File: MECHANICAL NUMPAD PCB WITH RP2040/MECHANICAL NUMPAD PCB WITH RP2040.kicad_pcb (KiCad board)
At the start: 4 copper layers, 76.2 x 95.2 mm, 46 parts, among them IC2 RP2040_QFN56, SW1 SW_Push, SW10 SW_Push, SW11 SW_Push, SW12 SW_Push, SW13 SW_Push, SW14 SW_Push, SW15 SW_Push, SW16 SW_Push, SW17 SW_Push, SW18 SW_Push, SW19 SW_Push, SW2 SW_Push, SW20 SW_Push, SW3 SW_Push, SW4 SW_Push, SW5 SW_Push, SW6 SW_Push, SW7 SW_Push, SW8 SW_Push, SW9 SW_Push, Y1 12MHZ

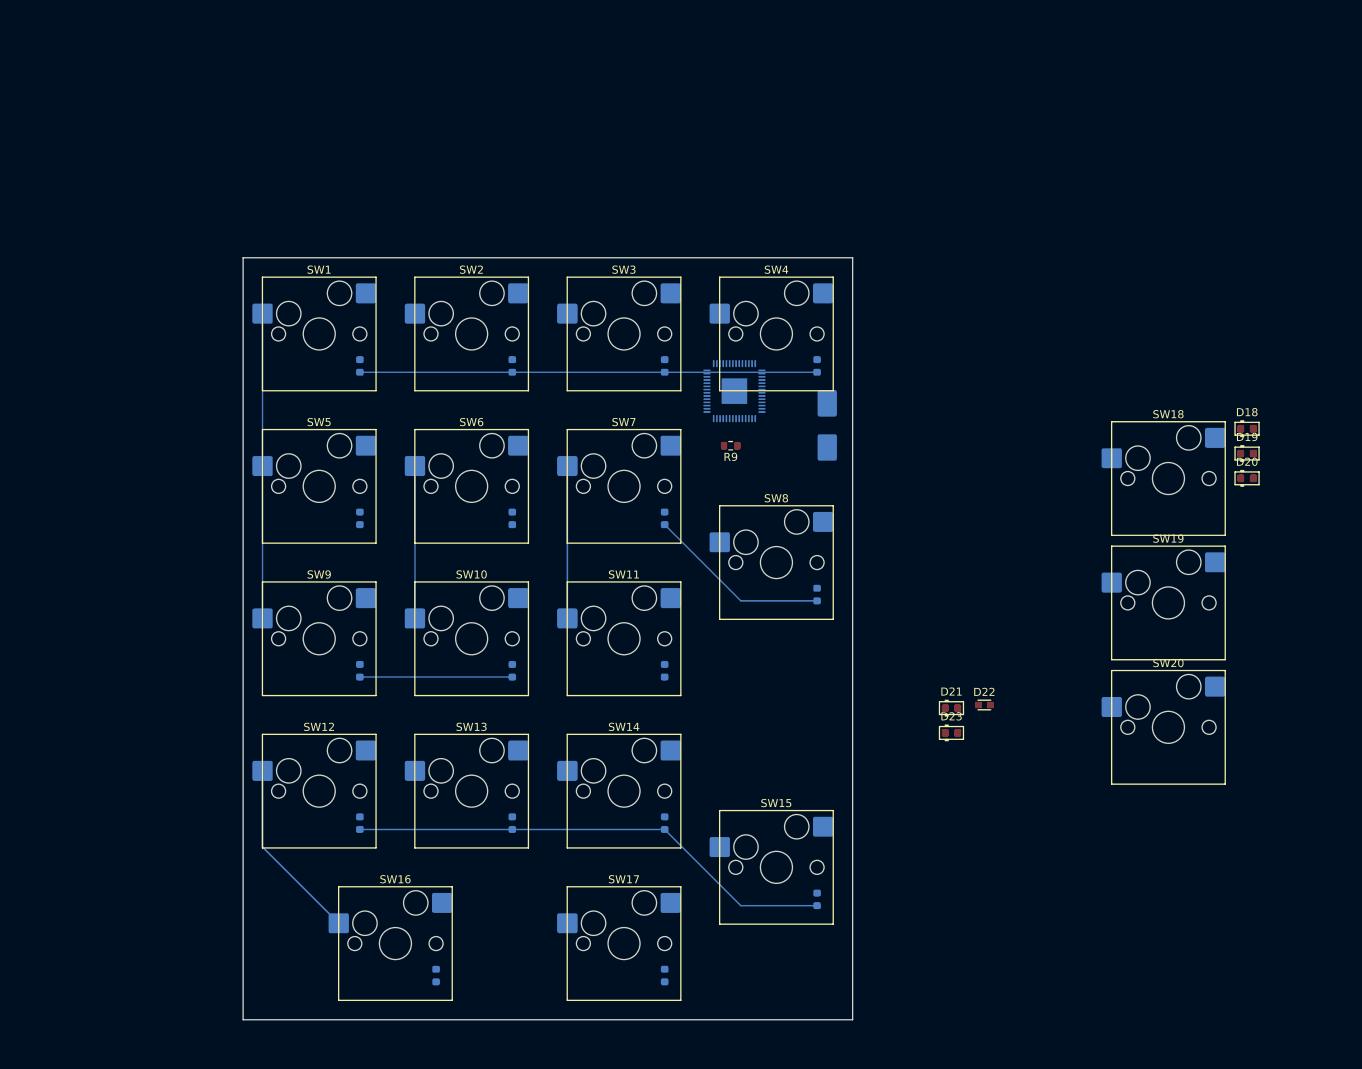
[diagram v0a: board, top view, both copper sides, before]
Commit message: Added footprints
Assigned footprints to all components, learned about bulk schematic symbol editing
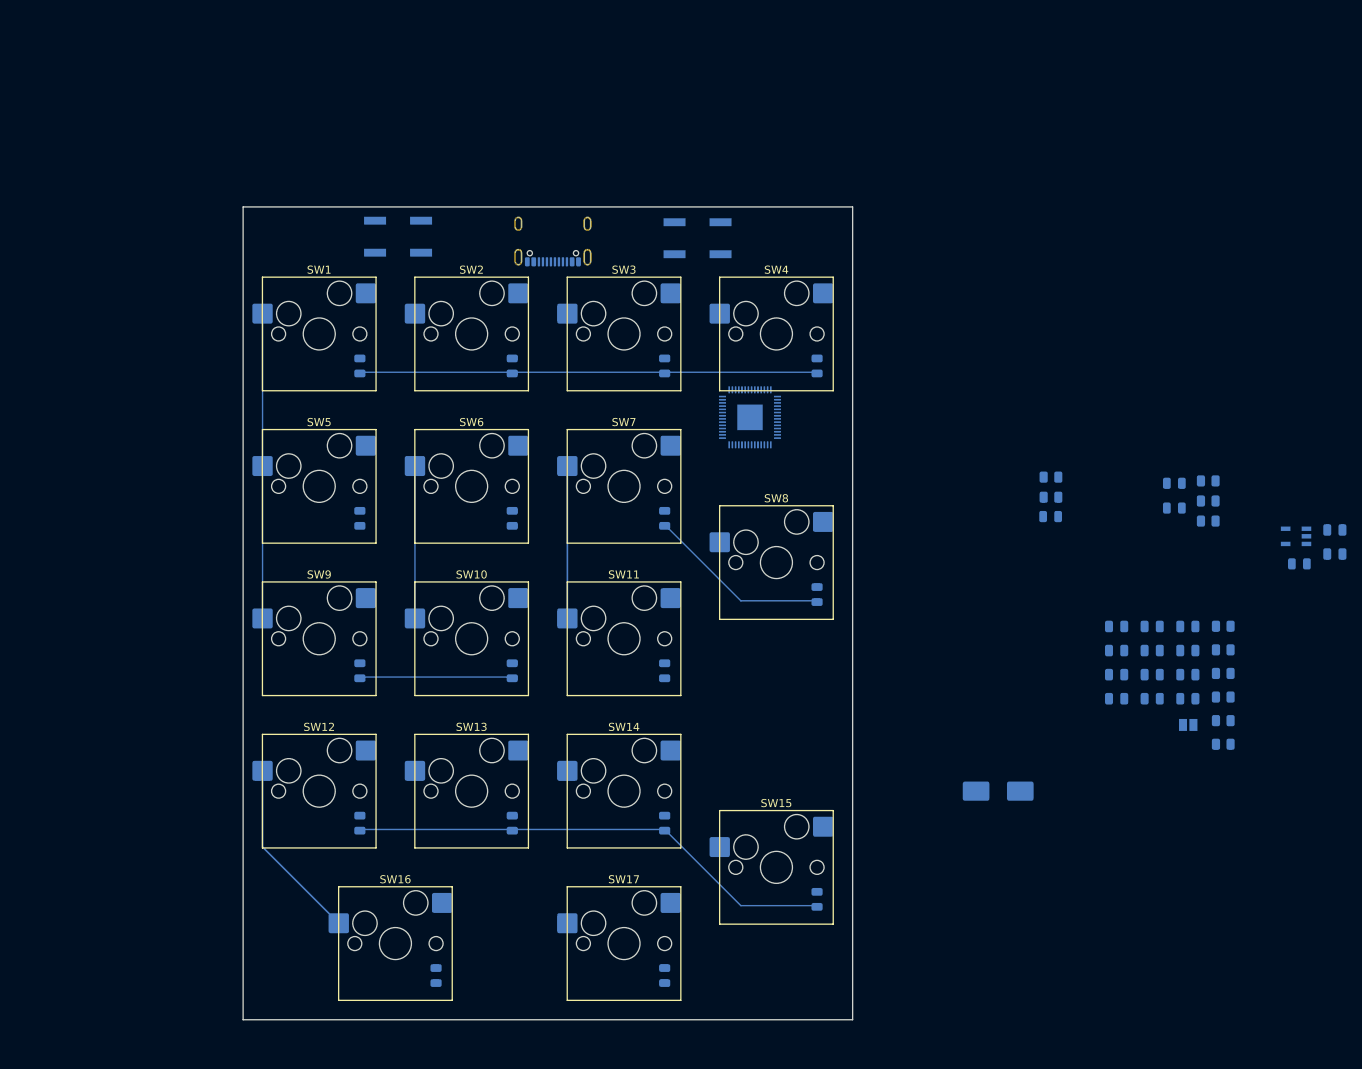
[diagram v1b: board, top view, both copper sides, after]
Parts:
- removed D18, D19, D20: CD4148WT, PCM_Diode_SMD_AKL:D_0603_1608Metric
- removed SW18, SW19, SW20: SW_Push, PCM_Switch_Keyboard_Hotswap_Kailh:SW_Hotswap_Kailh_MX_1.00u
- added C10: 1uF, Capacitor_SMD:C_0805_2012Metric, B.Cu at (146.7, 80.7)
- added C11: 0.1uF, Capacitor_SMD:C_0805_2012Metric, B.Cu at (146.7, 83.7)
- added C12: 1uF, Capacitor_SMD:C_0805_2012Metric, B.Cu at (142.2, 74.7)
- added C13: 0.1uF, Capacitor_SMD:C_0805_2012Metric, B.Cu at (142.2, 77.7)
- added C14: 0.1uF, Capacitor_SMD:C_0805_2012Metric, B.Cu at (142.2, 80.7)
- added C15: 1uF, Capacitor_SMD:C_0805_2012Metric, B.Cu at (142.2, 83.7)
- added C16: 0.1uF, Capacitor_SMD:C_0805_2012Metric, B.Cu at (137.8, 74.7)
- added C17: 0.1uF, Capacitor_SMD:C_0805_2012Metric, B.Cu at (137.8, 77.7)
- added C19: 22pF, Capacitor_SMD:C_0805_2012Metric, B.Cu at (137.8, 80.7)
- added C20: 22pF, Capacitor_SMD:C_0805_2012Metric, B.Cu at (137.8, 83.7)
- added C6: 10µF, Capacitor_SMD:C_0805_2012Metric, B.Cu at (165.1, 62.6)
- added C7: 0.1uF, Capacitor_SMD:C_0805_2012Metric, B.Cu at (146.7, 74.7)
- added C8: 10µF, Capacitor_SMD:C_0805_2012Metric, B.Cu at (165.1, 65.6)
- added C9: 0.1uF, Capacitor_SMD:C_0805_2012Metric, B.Cu at (146.7, 77.7)
- added J1: USB_C_Receptacle_USB2.0_16P, Connector_USB:USB_C_Receptacle_GCT_USB4105-xx-A_16P_TopMnt_Horizontal, B.Cu at (67.3, 25.4)
- added R1: 5.1K, Resistor_SMD:R_0805_2012Metric, B.Cu at (149.2, 56.5)
- added R10: 10K, Resistor_SMD:R_0805_2012Metric, B.Cu at (151.1, 86.4)
- added R11: 1K, Resistor_SMD:R_0805_2012Metric, B.Cu at (149.2, 61.5)
- added R12: 10K, Resistor_SMD:R_0805_2012Metric, B.Cu at (151.1, 89.4)
- added R2: 5.1K, Resistor_SMD:R_0805_2012Metric, B.Cu at (149.2, 59.0)
- added R3: 27, Resistor_SMD:R_0805_2012Metric, B.Cu at (151.1, 74.6)
- added R4: 27, Resistor_SMD:R_0805_2012Metric, B.Cu at (151.1, 77.6)
- added R5: 10K, Resistor_SMD:R_0805_2012Metric, B.Cu at (151.1, 80.5)
- added R6: 1K, Resistor_SMD:R_0805_2012Metric, B.Cu at (151.1, 83.5)
- added R7: 10K, Resistor_SMD:R_0805_2012Metric, B.Cu at (129.6, 56.0)
- added R8: FUSE, Fuse:Fuse_0805_2012Metric, B.Cu at (160.6, 66.8)
- added SJ1: SOLDERJUMPER, Jumper:SolderJumper-2_P1.3mm_Open_Pad1.0x1.5mm, B.Cu at (146.7, 87.0)
- added SW21: SKRAAKE010, JH_FOOTPRINTS:SW4_SKRAAKE010_ALPS, B.Cu at (48.0, 25.9)
- added SW22: SKRAAKE010, JH_FOOTPRINTS:SW4_SKRAAKE010_ALPS, B.Cu at (85.4, 26.1)
- added U2: AP2112K-3.3, PCM_SparkFun-Semiconductor-Standard:SOT23-5, B.Cu at (160.2, 63.4)
- D1, D10, D11, D12, D13, D14, D15, D16, D17, D2, D3, D4, D5, D6, D7, D8, D9: footprint PCM_Diode_SMD_AKL:D_0603_1608Metric -> PCM_Diode_SMD_AKL:D_0805_2012Metric
- D21, D23: footprint PCM_Diode_SMD_Handsoldering_AKL:D_0603_1608Metric -> PCM_Diode_SMD_AKL:D_0805_2012Metric; moved to B.Cu
- D22: footprint PCM_fab:LED_0603 -> PCM_LED_SMD_AKL:LED_0805_2012Metric; moved to B.Cu
- R9: footprint Resistor_SMD:R_0603_1608Metric -> Resistor_SMD:R_0805_2012Metric; moved to B.Cu
- moved Y1 50.5 mm to (123.0, 95.2), turned to 180 degrees
- moved R9 40.5 mm to (129.6, 58.5)
- moved D21 39.6 mm to (145.0, 56.8), turned to 180 degrees
- moved D23 39.6 mm to (145.0, 59.9), turned to 180 degrees
- moved D22 25.0 mm to (129.5, 60.9), turned to 180 degrees
- moved IC2 3.80 mm to (91.9, 48.5)
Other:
- board size 76.2 x 95.2 mm -> 76.2 x 101.6 mm

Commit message: Connecting components by matching symbol pin and footprint pad labels
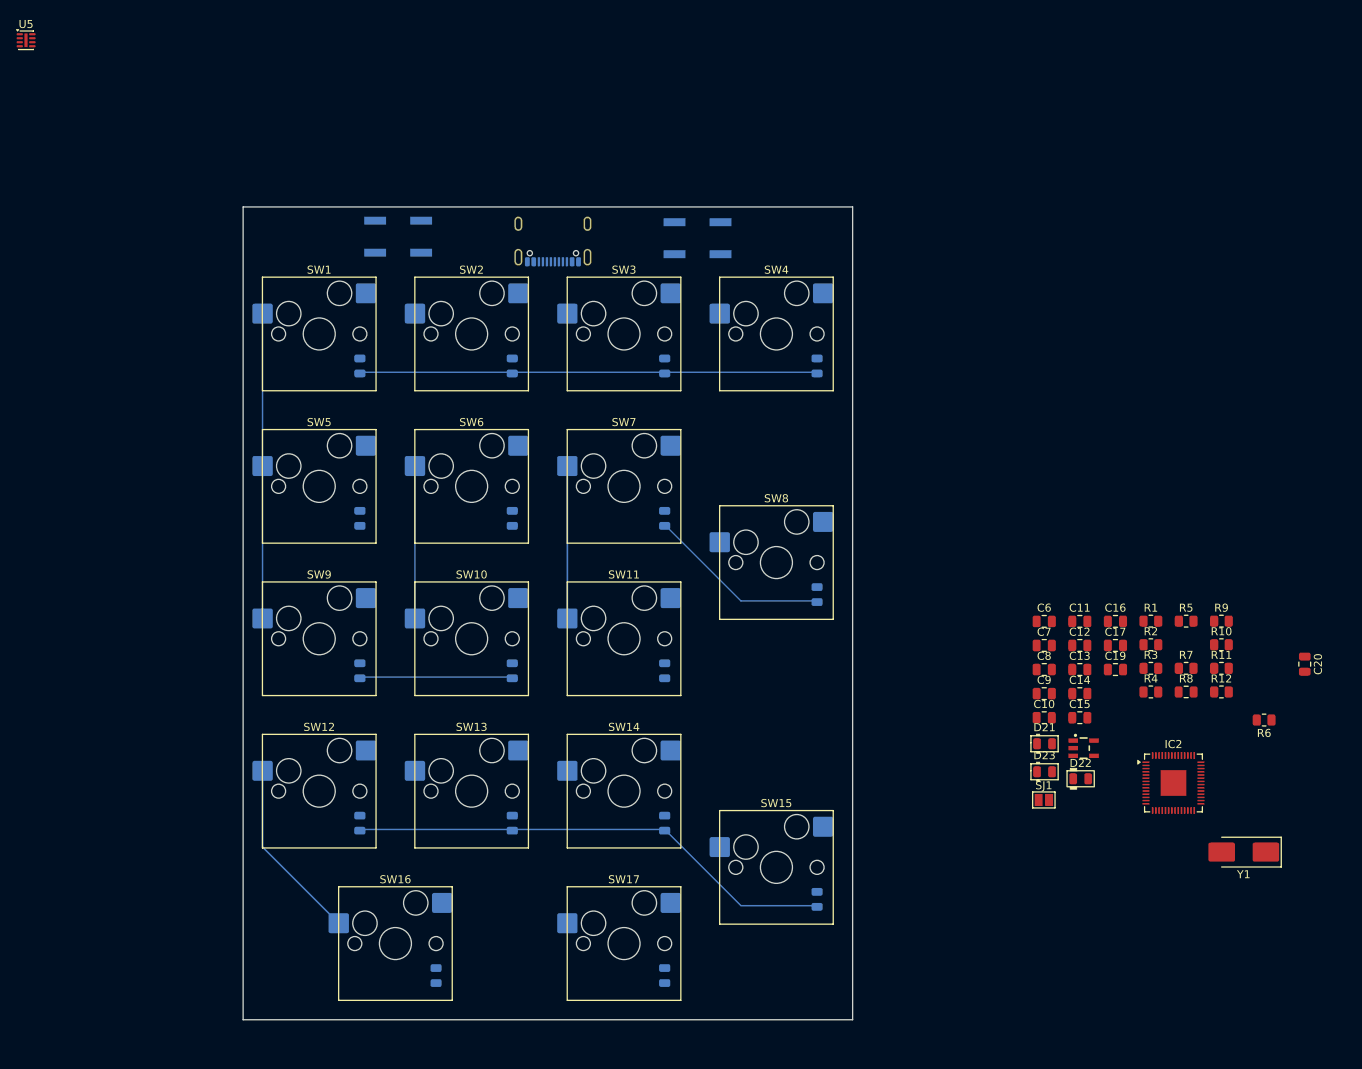
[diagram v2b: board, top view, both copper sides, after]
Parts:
- added U5: 8MB QSPI Flash, Package_SON:Texas_R-PUSON-N8_USON-8-1EP_1.6x2.1mm_P0.5mm_EP0.4x1.7mm, F.Cu at (1.46, 1.39)
- C10, C11, C12, C13, C14, C15, C16, C17, C19, C20, C6, C7, C8, C9, D21, D22, D23, IC2, R1, R10, R11, R12, R2, R3, R4, R5, R6, R7, R8, R9, SJ1, U2, Y1: moved to F.Cu
- moved IC2 69.9 mm to (144.9, 94.2), turned to 0 degrees
- moved C8 39.1 mm to (128.7, 80.0), turned to 0 degrees
- moved C6 38.1 mm to (128.7, 74.0), turned to 0 degrees
- moved U2 37.5 mm to (133.6, 89.9), turned to 0 degrees
- moved D23 36.7 mm to (128.8, 92.8), turned to 0 degrees
- moved D21 36.4 mm to (128.8, 89.3), turned to 0 degrees
- moved D22 33.0 mm to (133.3, 93.7), turned to 0 degrees
- moved Y1 31.6 mm to (153.7, 102.9)
- moved R7 29.3 mm to (146.5, 79.9), turned to 0 degrees
- moved R9 26.3 mm to (150.9, 74.0), turned to 0 degrees
- moved C20 23.9 mm to (161.3, 79.4), turned to -90 degrees
- moved R8 21.4 mm to (146.5, 82.8), turned to 0 degrees
- moved SJ1 20.3 mm to (128.7, 96.3), turned to 0 degrees
- moved R2 19.3 mm to (142.1, 77.0), turned to 0 degrees
- moved R1 18.9 mm to (142.1, 74.0), turned to 0 degrees
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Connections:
- Y1 pad 2: (no net) -> Net-(IC2-XIN)

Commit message: Refinement of schematic and PCB
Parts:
- C10, C11, C12, C13, C14, C15, C16, C17, C19, C20, C6, C7, C8, C9: footprint Capacitor_SMD:C_0805_2012Metric -> Capacitor_SMD:C_0603_1608Metric; moved to B.Cu
- D1, D10, D11, D12, D13, D14, D15, D16, D17, D2, D3, D4, D5, D6, D7, D8, D9: value CD4148WT -> TS4148
- D21: value NSR0320 -> TS4148; moved to B.Cu
- D22: footprint PCM_LED_SMD_AKL:LED_0805_2012Metric -> PCM_SparkFun-LED:LED_0603_1608Metric_Green; moved to B.Cu
- D23: value NSR0320 -> TS4148
- IC2, U2: moved to B.Cu
- R1, R10, R11, R12, R2, R3, R4, R5, R6, R7, R9: footprint Resistor_SMD:R_0805_2012Metric -> Resistor_SMD:R_0603_1608Metric; moved to B.Cu
- R8: footprint Fuse:Fuse_0805_2012Metric -> Fuse:Fuse_0603_1608Metric; moved to B.Cu
- U5: footprint Package_SON:Texas_R-PUSON-N8_USON-8-1EP_1.6x2.1mm_P0.5mm_EP0.4x1.7mm -> PCM_SparkFun-Semiconductor-Standard:USON-8_3x2mm-SkinnyCenterPad; moved to B.Cu
- Y1: footprint Crystal:Crystal_SMD_Abracon_ABM3-2Pin_5.0x3.2mm_HandSoldering -> Crystal:Crystal_SMD_3215-2Pin_3.2x1.5mm; moved to B.Cu
- moved U5 126.0 mm to (100.3, 79.5), turned to 90 degrees
- moved R2 98.8 mm to (58.3, 24.5), turned to 180 degrees
- moved R1 96.1 mm to (58.1, 27.3), turned to 180 degrees
- moved C20 91.5 mm to (70.0, 85.6), turned to 90 degrees
- moved R6 89.9 mm to (66.3, 85.6), turned to -90 degrees
- moved SJ1 85.6 mm to (79.3, 26.3), turned to -90 degrees
- moved R8 78.6 mm to (90.2, 27.9)
- moved U2 75.8 mm to (94.8, 24.8)
- moved D22 74.5 mm to (98.0, 28.0)
- moved R11 73.3 mm to (102.8, 24.6)
- moved R7 72.8 mm to (99.2, 24.5)
- moved D21 70.6 mm to (94.0, 27.9)
- moved C8 70.0 mm to (86.1, 24.5)
- moved D23 68.7 mm to (102.0, 29.5)
- moved R3 65.1 mm to (91.2, 120.6), turned to -90 degrees
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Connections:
- D21 pad 1: (no net) -> /RAW
- D21 pad 2: (no net) -> Net-(D21-A)
- D22 pad 1: (no net) -> 3.3V
- D22 pad 2: (no net) -> Net-(D22-C)
- D23 pad 1: (no net) -> /USBBOOT
- D23 pad 2: (no net) -> Net-(D23-A)
- D4 pad 1: /ROW1 -> unconnected-(D4-K-Pad1)
- D4 pad 2: Net-(D4-A) -> unconnected-(D4-A-Pad2)
- IC2 pad 14: /USBBOOT -> /USB_BOOT
- IC2 pad 57: (no net) -> GND
- J1 pad SH: unconnected-(J1-SHIELD-PadSH) -> GND
- R11 pad 2: Net-(D23-PadA) -> Net-(D23-A)
- R7 pad 1: Net-(D22-PadC) -> Net-(D22-C)
- R8 pad 2: Net-(D21-PadA) -> Net-(D21-A)
- SW4 pad 2: Net-(D4-A) -> unconnected-(SW4-Pad2)
- U5 pad 9: (no net) -> GND
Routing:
- net 3.3V: track 0.00 -> 73.3 mm, vias 0 -> 2
- net /COL1: track 38.1 -> 110.4 mm
- net /ROW2: track 103.1 -> 170.3 mm
- net /USB_BOOT: track 0.00 -> 57.6 mm, vias 0 -> 1
- net VBUS: track 0.00 -> 45.6 mm, vias 0 -> 1
- net /~{RESET}: track 0.00 -> 41.2 mm, vias 0 -> 2
- net /COL4: track 23.0 -> 51.7 mm, vias 0 -> 2
- net /RAW: track 0.00 -> 22.8 mm, vias 0 -> 1
- net /ROW1: track 57.1 -> 38.1 mm
- net Net-(C20-Pad2): track 0.00 -> 16.0 mm
- net Net-(J1-CC2): track 0.00 -> 12.4 mm
- net /QSPI_DATA[3]: track 0.00 -> 10.1 mm
- net Net-(D11-A): track 0.00 -> 9.47 mm
- net Net-(J1-CC1): track 0.00 -> 9.05 mm
- net Net-(D15-A): track 0.00 -> 8.84 mm
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- added copper zone on B.Cu, net GND
- added copper zone on F.Cu, net GND

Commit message: Finished PCB
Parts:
- D23: moved to B.Cu
- moved R12 47.4 mm to (88.7, 95.5), turned to 180 degrees
- moved R10 46.0 mm to (85.7, 94.1), turned to -90 degrees
- moved R3 45.1 mm to (102.6, 76.9), turned to 90 degrees
- moved R4 44.1 mm to (100.8, 76.9), turned to 90 degrees
- moved R9 27.7 mm to (98.5, 77.0)
- moved R6 27.6 mm to (92.5, 77.0)
- moved C20 25.3 mm to (92.5, 73.9), turned to -90 degrees
- moved R5 23.6 mm to (102.6, 28.5), turned to 180 degrees
- moved C14 21.5 mm to (101.4, 93.4), turned to 0 degrees
- moved Y1 21.1 mm to (89.2, 76.9), turned to 90 degrees
- moved C11 18.7 mm to (96.2, 77.0), turned to -90 degrees
- moved C7 18.6 mm to (92.5, 95.0), turned to 90 degrees
- moved C13 18.1 mm to (94.1, 77.0), turned to 90 degrees
- moved C19 17.8 mm to (90.1, 79.8), turned to 180 degrees
- moved U5 17.1 mm to (89.2, 92.5), turned to -90 degrees
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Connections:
- D10 pad 1: /ROW2 -> /ROW3
- D11 pad 1: /ROW2 -> /ROW3
- D12 pad 1: /ROW2 -> /ROW3
- D13 pad 1: /ROW2 -> /ROW4
- D14 pad 1: /ROW2 -> /ROW4
- D15 pad 1: /ROW2 -> /ROW4
- D16 pad 1: /ROW2 -> /ROW4
- D17 pad 1: /ROW2 -> /ROW5
- D23 pad 1: /USBBOOT -> /USB_BOOT
- D4 pad 1: unconnected-(D4-K-Pad1) -> /ROW1
- D4 pad 2: unconnected-(D4-A-Pad2) -> Net-(D4-A)
- D9 pad 1: /ROW2 -> /ROW3
- SW22 pad 1: /USBBOOT -> /USB_BOOT
- SW22 pad 3: /USBBOOT -> /USB_BOOT
- SW4 pad 2: unconnected-(SW4-Pad2) -> Net-(D4-A)
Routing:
- net /~{RESET}: track 41.2 -> 140.9 mm, vias 2 -> 0
- net /ROW4: track 0.00 -> 92.7 mm, vias 0 -> 4
- net /COL4: track 51.7 -> 140.0 mm, vias 2 -> 3
- net /ROW3: track 0.00 -> 88.0 mm, vias 0 -> 2
- net /QSPI_CS: track 5.42 -> 90.4 mm, vias 0 -> 2
- net /COL2: track 19.0 -> 103.3 mm, vias 0 -> 2
- net /ROW1: track 38.1 -> 112.4 mm, vias 0 -> 2
- net /D+: track 0.00 -> 73.7 mm, vias 0 -> 2
- net /COL3: track 19.0 -> 92.6 mm, vias 0 -> 6
- net /D-: track 0.00 -> 73.4 mm, vias 0 -> 2
- net /ROW2: track 170.3 -> 119.1 mm, vias 0 -> 4
- net /COL1: track 110.4 -> 160.6 mm
- net 3.3V: track 73.3 -> 24.2 mm, vias 2 -> 21
- net /ROW5: track 0.00 -> 42.6 mm, vias 0 -> 2
- net 1.2V: track 4.88 -> 29.9 mm, vias 0 -> 5
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- added copper zone on In1.Cu, net 3.3V
- added copper zone on In2.Cu, net 3.3V

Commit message: In progress of adding Neopixels
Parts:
- added D18: NEOP, LED_SMD:LED_SK6812MINI-E_3.2x2.8mm_P1.5mm_ReverseMount, F.Cu at (126.8, 43.7)
- added D19: NEOP, LED_SMD:LED_SK6812MINI-E_3.2x2.8mm_P1.5mm_ReverseMount, F.Cu at (126.8, 48.6)
- added D20: NEOP, LED_SMD:LED_SK6812MINI-E_3.2x2.8mm_P1.5mm_ReverseMount, F.Cu at (126.8, 53.4)
- added D24: NEOP, LED_SMD:LED_SK6812MINI-E_3.2x2.8mm_P1.5mm_ReverseMount, F.Cu at (126.8, 58.3)
- added D25: NEOP, LED_SMD:LED_SK6812MINI-E_3.2x2.8mm_P1.5mm_ReverseMount, F.Cu at (126.8, 63.2)
- added D26: NEOP, LED_SMD:LED_SK6812MINI-E_3.2x2.8mm_P1.5mm_ReverseMount, F.Cu at (135.2, 43.7)
- added D27: NEOP, LED_SMD:LED_SK6812MINI-E_3.2x2.8mm_P1.5mm_ReverseMount, F.Cu at (135.2, 48.6)
- added D28: NEOP, LED_SMD:LED_SK6812MINI-E_3.2x2.8mm_P1.5mm_ReverseMount, F.Cu at (135.2, 53.4)
- added D29: NEOP, LED_SMD:LED_SK6812MINI-E_3.2x2.8mm_P1.5mm_ReverseMount, F.Cu at (135.2, 58.3)
- added D30: NEOP, LED_SMD:LED_SK6812MINI-E_3.2x2.8mm_P1.5mm_ReverseMount, F.Cu at (135.2, 63.2)
- added D31: NEOP, LED_SMD:LED_SK6812MINI-E_3.2x2.8mm_P1.5mm_ReverseMount, F.Cu at (143.6, 43.7)
- added D32: NEOP, LED_SMD:LED_SK6812MINI-E_3.2x2.8mm_P1.5mm_ReverseMount, F.Cu at (143.6, 48.6)
- added D33: NEOP, LED_SMD:LED_SK6812MINI-E_3.2x2.8mm_P1.5mm_ReverseMount, F.Cu at (143.6, 53.4)
- added D34: NEOP, LED_SMD:LED_SK6812MINI-E_3.2x2.8mm_P1.5mm_ReverseMount, F.Cu at (143.6, 58.3)
- added D35: NEOP, LED_SMD:LED_SK6812MINI-E_3.2x2.8mm_P1.5mm_ReverseMount, F.Cu at (143.6, 63.2)
- added D36: NEOP, LED_SMD:LED_SK6812MINI-E_3.2x2.8mm_P1.5mm_ReverseMount, F.Cu at (152.1, 43.7)
- added D37: NEOP, LED_SMD:LED_SK6812MINI-E_3.2x2.8mm_P1.5mm_ReverseMount, F.Cu at (152.1, 48.6)
- added D38: NEOP, LED_SMD:LED_SK6812MINI-E_3.2x2.8mm_P1.5mm_ReverseMount, F.Cu at (152.1, 53.4)
- added D39: NEOP, LED_SMD:LED_SK6812MINI-E_3.2x2.8mm_P1.5mm_ReverseMount, F.Cu at (152.1, 58.3)
- added D40: NEOP, LED_SMD:LED_SK6812MINI-E_3.2x2.8mm_P1.5mm_ReverseMount, F.Cu at (152.1, 63.2)
- added R13: 200K, Resistor_SMD:R_0603_1608Metric, F.Cu at (130.2, 66.9)
- added U1: LVL SHFTR, Package_SO:VSSOP-8_2.3x2mm_P0.5mm, F.Cu at (125.4, 75.0)
